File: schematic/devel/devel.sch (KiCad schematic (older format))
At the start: 40 parts, among them J1 CONN_PWR, J2 CONN_X1, J3 CONN_Y2, J4 CONN_X2, J5 CONN_Y1, U1 L7812, U2 L7912, U3 REF5010IDGK, U4 OPA4197

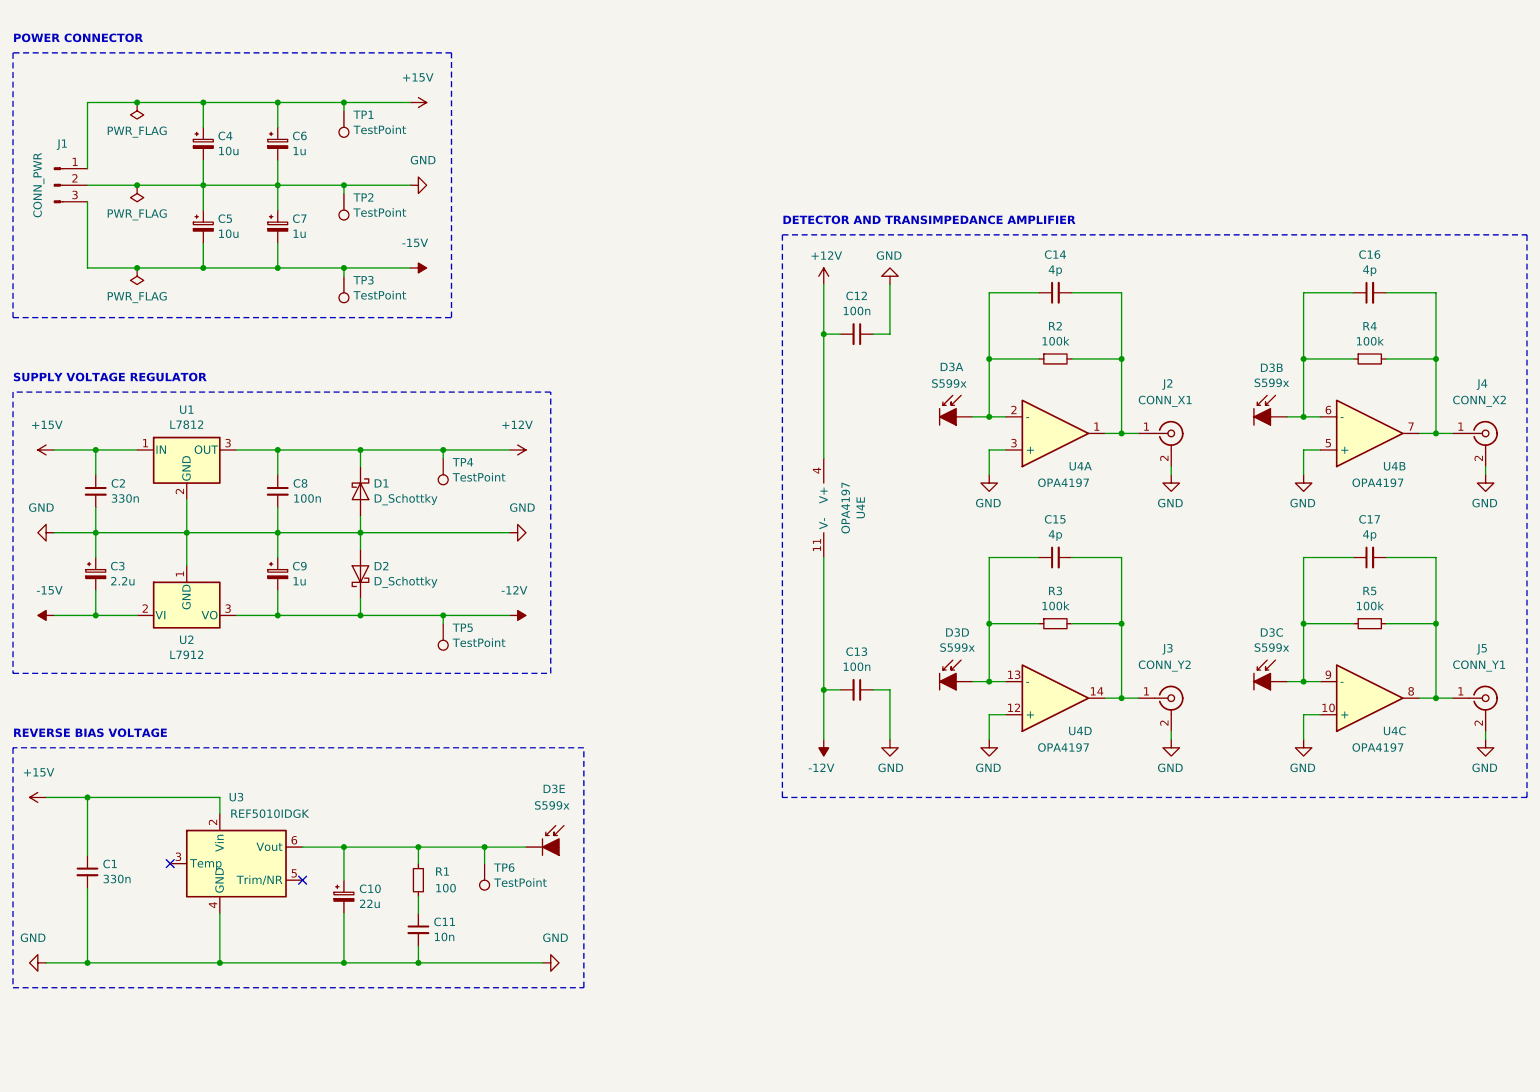
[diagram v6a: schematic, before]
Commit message: simplified circuit schematic, used uniform resistor footprints
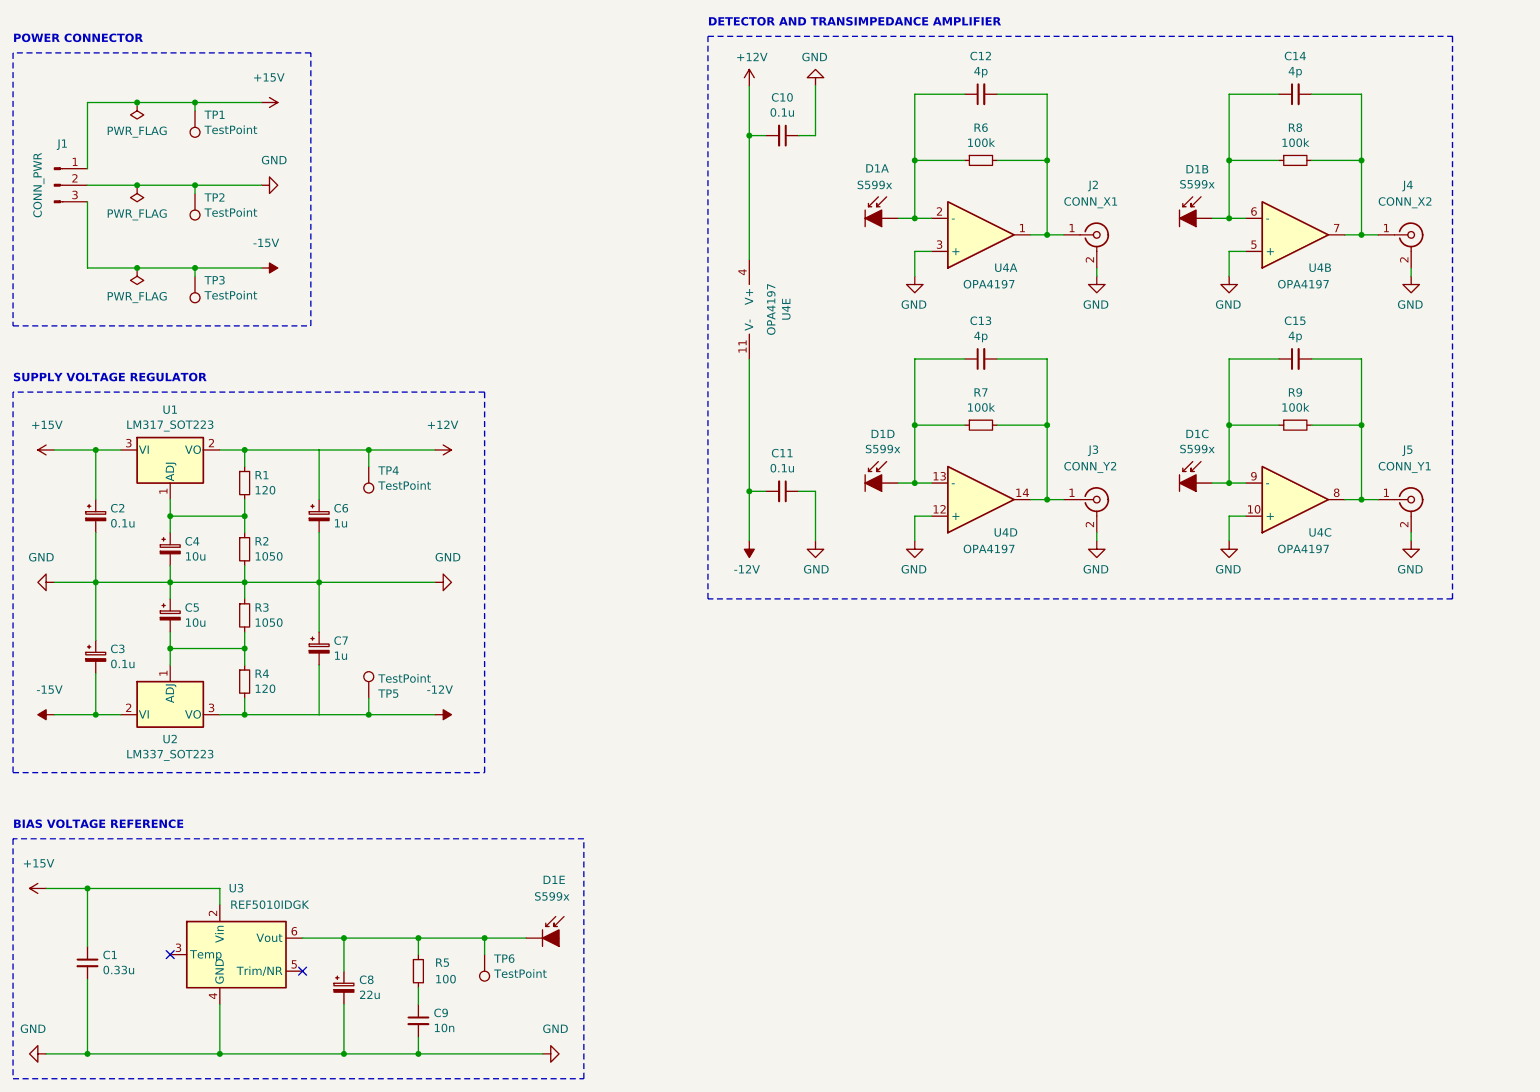
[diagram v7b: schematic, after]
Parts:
- removed C2: 330n, Capacitor_SMD:C_0805_2012Metric, symbol Device:C_Small
- removed C8: 100n, Capacitor_SMD:C_0603_1608Metric, symbol Device:C_Small
- removed C9: 1u, Capacitor_SMD:CP_Elec_5x4.4, symbol Device:CP_Small
- removed D1, D2: D_Schottky, Diode_SMD:D_SMA, symbol Device:D_Schottky
- removed U1: L7812, Package_TO_SOT_SMD:TO-252-2, symbol Regulator_Linear:L7812
- removed U2: L7912, Package_TO_SOT_SMD:TO-252-2, symbol Regulator_Linear:L7912
- added C2: 0.1u, Capacitor_SMD:CP_Elec_4x3.9, symbol Device:CP_Small
- added R1, R4: 120, Resistor_SMD:R_0805_2012Metric, symbol Device:R_Small
- added R2, R3: 1050, Resistor_SMD:R_0805_2012Metric, symbol Device:R_Small
- added U1: LM317_SOT223, Package_TO_SOT_SMD:SOT-223-3_TabPin2, symbol Regulator_Linear:LM317_3PinPackage
- added U2: LM337_SOT223, Package_TO_SOT_SMD:SOT-223-3_TabPin2, symbol Regulator_Linear:LM337_SOT223
- C1: value 330n -> 0.33u
- C10: renamed from C12; value 100n -> 0.1u; footprint Capacitor_SMD:C_0201_0603Metric -> Capacitor_SMD:C_0603_1608Metric
- C11: renamed from C13; value 100n -> 0.1u; footprint Capacitor_SMD:C_0201_0603Metric -> Capacitor_SMD:C_0603_1608Metric
- C3: value 2.2u -> 0.1u; footprint Capacitor_SMD:CP_Elec_4x5.4 -> Capacitor_SMD:CP_Elec_4x3.9
- C4, C5, C6, C7: footprint Capacitor_SMD:CP_Elec_4x5.4 -> Capacitor_SMD:CP_Elec_4x3.9
- C9: renamed from C11; footprint Capacitor_SMD:C_0402_1005Metric -> Capacitor_SMD:C_0603_1608Metric
- J1: footprint Connector_PinHeader_2.00mm:PinHeader_1x03_P2.00mm_Vertical_SMD_Pin1Left -> Connector_PinHeader_1.00mm:PinHeader_1x03_P1.00mm_Vertical_SMD_Pin1Left
- R5: renamed from R1; footprint Resistor_SMD:R_0603_1608Metric -> Resistor_SMD:R_0805_2012Metric
- renumbered C14 to C12, C15 to C13, C16 to C14, C17 to C15, C10 to C8, D3 to D1, R2 to R6, R3 to R7, R4 to R8, R5 to R9
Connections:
- net +12V: now also C6.1, R1.1, U1.2 (VO)
- net +15V: now also C2.1, U1.3 (VI); no longer C4.1, C6.1
- net -12V: now also C7.2, R4.2, U2.3 (VO)
- net -15V: now also U2.2 (VI); no longer C5.2, C7.2
- net GND: now also C2.2, R2.2, R3.1
- new net: C5.2, R3.2, R4.1, U2.1 (ADJ)
- new net: C4.1, R1.2, R2.1, U1.1 (ADJ)
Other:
- note added: "BIAS VOLTAGE REFERENCE"
- note removed: "REVERSE BIAS VOLTAGE"
- moved on the sheet: C1, C10, C11, C12, C13, C14, C15, C8, C9, D1A, D1B, D1C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

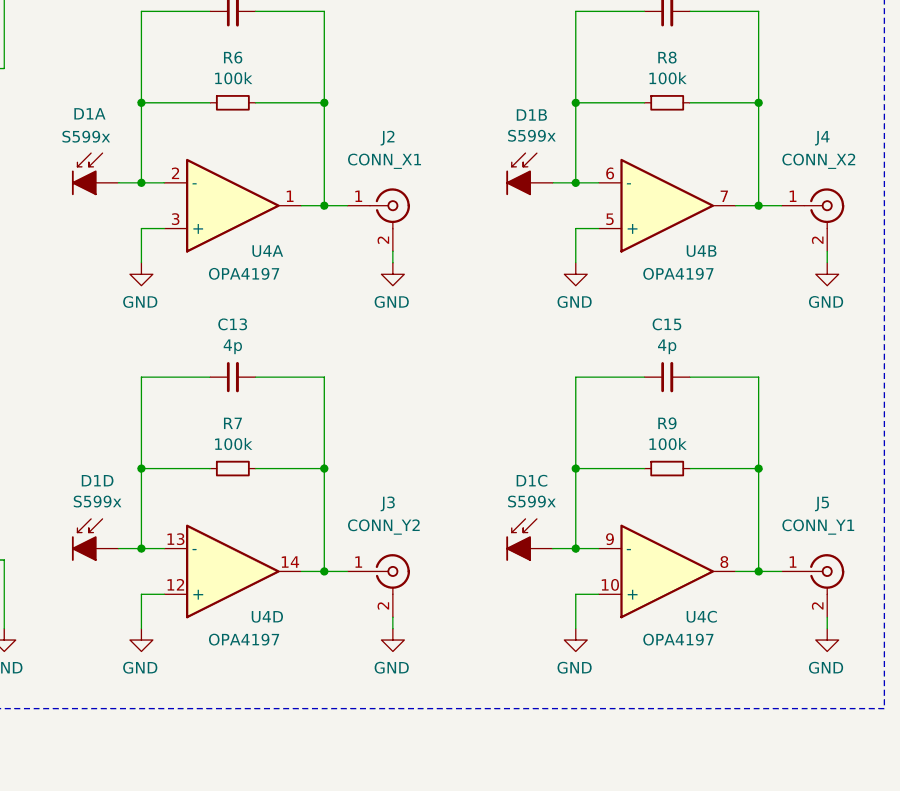
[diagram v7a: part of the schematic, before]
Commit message: completed sublayout of detector and preamp
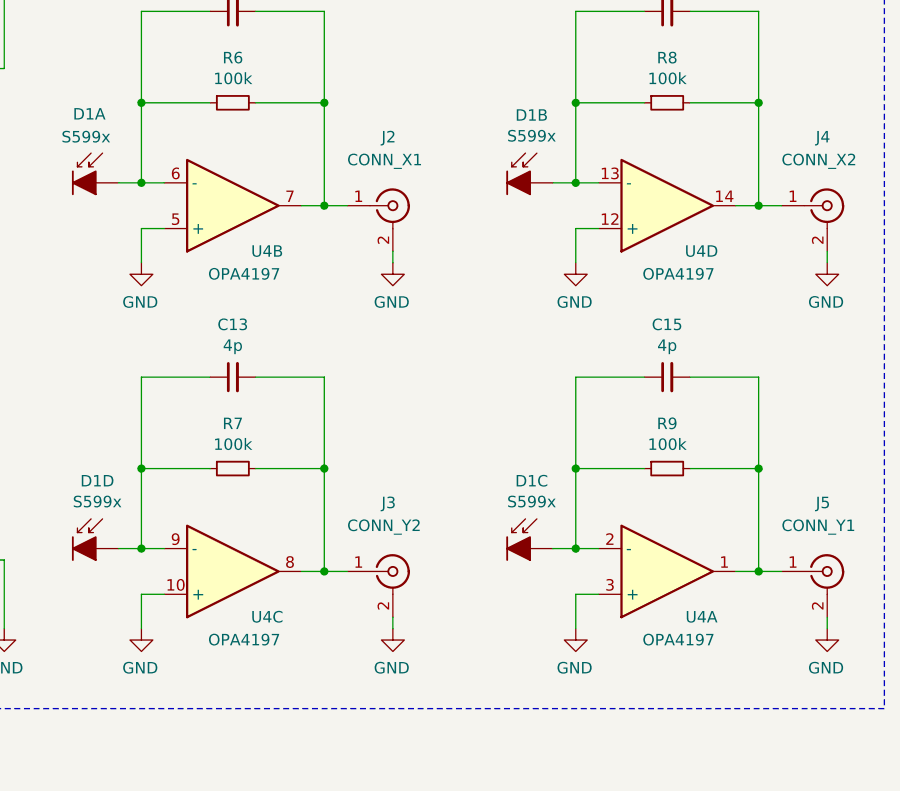
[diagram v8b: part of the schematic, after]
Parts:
- C10, C11: footprint Capacitor_SMD:C_0603_1608Metric -> Capacitor_SMD:C_0402_1005Metric
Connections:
- net at C12.1, D1.1 (I1), R6.1: now also U4.6 (-); no longer U4.2 (-)
- net at C14.1, D1.6 (I2), R8.1: now also U4.13 (-); no longer U4.6 (-)
- net at C14.2, J4.1 (In), R8.2: now also U4.14; no longer U4.7
- net at C15.1, D1.10 (I4), R9.1: now also U4.2 (-); no longer U4.9 (-)
- net at C15.2, J5.1 (In), R9.2: now also U4.1; no longer U4.8
- net at C12.2, J2.1 (In), R6.2: now also U4.7; no longer U4.1
- net at C13.1, D1.5 (I3), R7.1: now also U4.9 (-); no longer U4.13 (-)
- net at C13.2, J3.1 (In), R7.2: now also U4.8; no longer U4.14
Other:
- moved on the sheet: U4A, U4B, U4C, U4D
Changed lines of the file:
@@
 L Device:Opamp_Quad_Generic U4
 U 2 1 5C9FE32B
-P 8650 2050
+P 6750 2050
 AR Path="/5C9FE32B" Ref="U4"  Part="2"
 AR Path="/5D929D0E/5C9FE32B" Ref="U?"  Part="2"
-F 0 "U4" H 8800 2250 50  0000 C CNN
-F 1 "OPA4197" H 8700 2350 50  0000 C CNN
-F 2 "Package_SO:TSSOP-14_4.4x5mm_P0.65mm" H 8650 2050 50  0001 C CNN
-F 3 "~" H 8650 2050 50  0001 C CNN
-	2    8650 2050
+F 0 "U4" H 6900 2250 50  0000 C CNN
+F 1 "OPA4197" H 6800 2350 50  0000 C CNN
+F 2 "Package_SO:TSSOP-14_4.4x5mm_P0.65mm" H 6750 2050 50  0001 C CNN
+F 3 "~" H 6750 2050 50  0001 C CNN
+	2    6750 2050
 	1    0    0    1
 $EndComp
@@
 L Device:Opamp_Quad_Generic U4
 U 3 1 5C9FE357
-P 8650 3650
+P 6750 3650
 AR Path="/5C9FE357" Ref="U4"  Part="3"
 AR Path="/5D929D0E/5C9FE357" Ref="U?"  Part="3"
-F 0 "U4" H 8800 3850 50  0000 C CNN
-F 1 "OPA4197" H 8700 3950 50  0000 C CNN
-F 2 "Package_SO:TSSOP-14_4.4x5mm_P0.65mm" H 8650 3650 50  0001 C CNN
-F 3 "~" H 8650 3650 50  0001 C CNN
-	3    8650 3650
+F 0 "U4" H 6900 3850 50  0000 C CNN
+F 1 "OPA4197" H 6800 3950 50  0000 C CNN
+F 2 "Package_SO:TSSOP-14_4.4x5mm_P0.65mm" H 6750 3650 50  0001 C CNN
+F 3 "~" H 6750 3650 50  0001 C CNN
+	3    6750 3650
 	1    0    0    1
 $EndComp
@@
 L Device:Opamp_Quad_Generic U4
 U 1 1 5C9FE382
-P 6750 2050
+P 8650 3650
 AR Path="/5C9FE382" Ref="U4"  Part="1"
 AR Path="/5D929D0E/5C9FE382" Ref="U?"  Part="1"
-F 0 "U4" H 6900 2250 50  0000 C CNN
-F 1 "OPA4197" H 6800 2350 50  0000 C CNN
-F 2 "Package_SO:TSSOP-14_4.4x5mm_P0.65mm" H 6750 2050 50  0001 C CNN
-F 3 "~" H 6750 2050 50  0001 C CNN
-	1    6750 2050
+F 0 "U4" H 8800 3850 50  0000 C CNN
+F 1 "OPA4197" H 8700 3950 50  0000 C CNN
+F 2 "Package_SO:TSSOP-14_4.4x5mm_P0.65mm" H 8650 3650 50  0001 C CNN
+F 3 "~" H 8650 3650 50  0001 C CNN
+	1    8650 3650
 	1    0    0    1
 $EndComp
@@
 L Device:Opamp_Quad_Generic U4
 U 4 1 5C9FE388
-P 6750 3650
+P 8650 2050
 AR Path="/5C9FE388" Ref="U4"  Part="4"
 AR Path="/5D929D0E/5C9FE388" Ref="U?"  Part="4"
-F 0 "U4" H 6900 3850 50  0000 C CNN
-F 1 "OPA4197" H 6800 3950 50  0000 C CNN
-F 2 "Package_SO:TSSOP-14_4.4x5mm_P0.65mm" H 6750 3650 50  0001 C CNN
-F 3 "~" H 6750 3650 50  0001 C CNN
-	4    6750 3650
+F 0 "U4" H 8800 2250 50  0000 C CNN
+F 1 "OPA4197" H 8700 2350 50  0000 C CNN
+F 2 "Package_SO:TSSOP-14_4.4x5mm_P0.65mm" H 8650 2050 50  0001 C CNN
+F 3 "~" H 8650 2050 50  0001 C CNN
+	4    8650 2050
 	1    0    0    1
 $EndComp
@@
 F 0 "C10" V 5321 1450 50  0000 C CNN
 F 1 "0.1u" V 5412 1450 50  0000 C CNN
-F 2 "Capacitor_SMD:C_0603_1608Metric" H 5550 1450 50  0001 C CNN
+F 2 "Capacitor_SMD:C_0402_1005Metric" H 5550 1450 50  0001 C CNN
 F 3 "~" H 5550 1450 50  0001 C CNN
 	1    5550 1450
@@
 F 0 "C11" V 5321 3600 50  0000 C CNN
 F 1 "0.1u" V 5412 3600 50  0000 C CNN
-F 2 "Capacitor_SMD:C_0603_1608Metric" H 5550 3600 50  0001 C CNN
+F 2 "Capacitor_SMD:C_0402_1005Metric" H 5550 3600 50  0001 C CNN
 F 3 "~" H 5550 3600 50  0001 C CNN
 	1    5550 3600
